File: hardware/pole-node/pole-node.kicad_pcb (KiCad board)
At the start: 2 copper layers, 50.5 x 33.5 mm, 31 parts, among them J1 Anderson, J2 RJ45, J3 Conn_01x02, J4 Conn_01x03, J5 Conn_01x03, J6 Conn_01x03, U1 AP3211, U2 MAX485E, U3 MAX485E

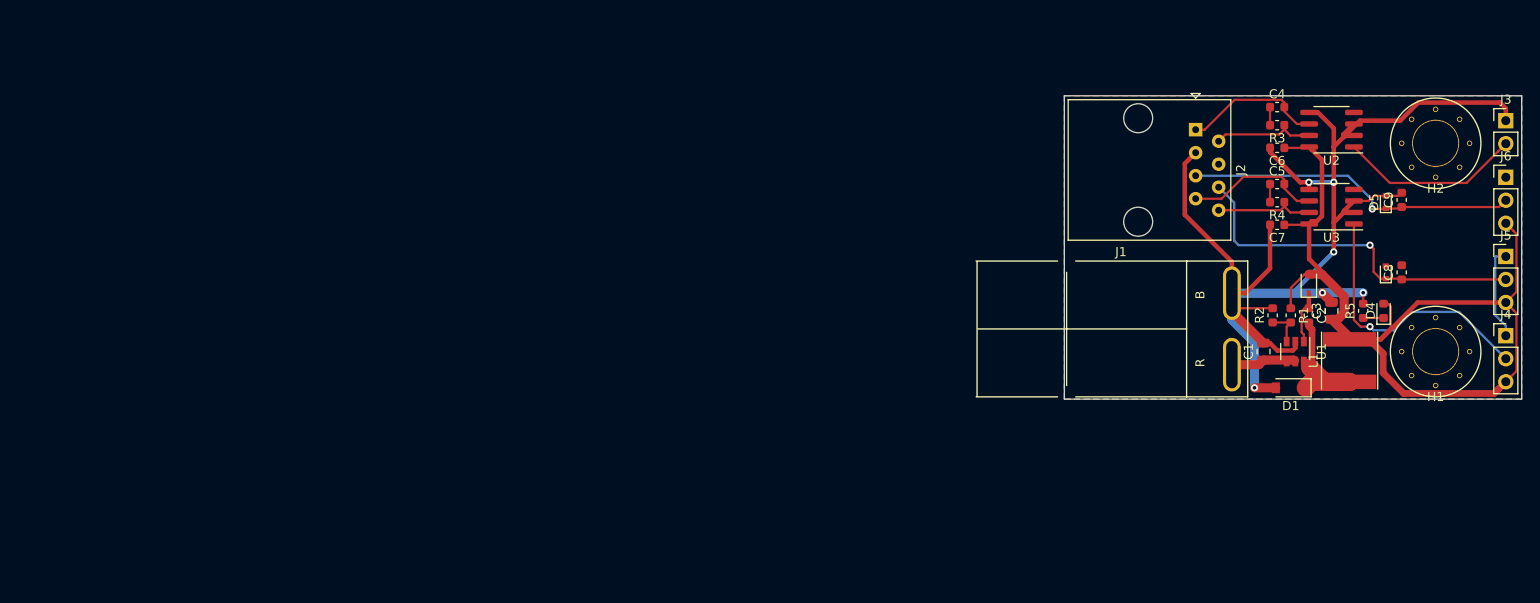
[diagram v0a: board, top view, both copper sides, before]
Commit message: Update pole node to v1.1
This adds lots of TVS diode, more decoupling, bulk caps on 5v and 12v
lines. Also adds pass-through Anderson connector.
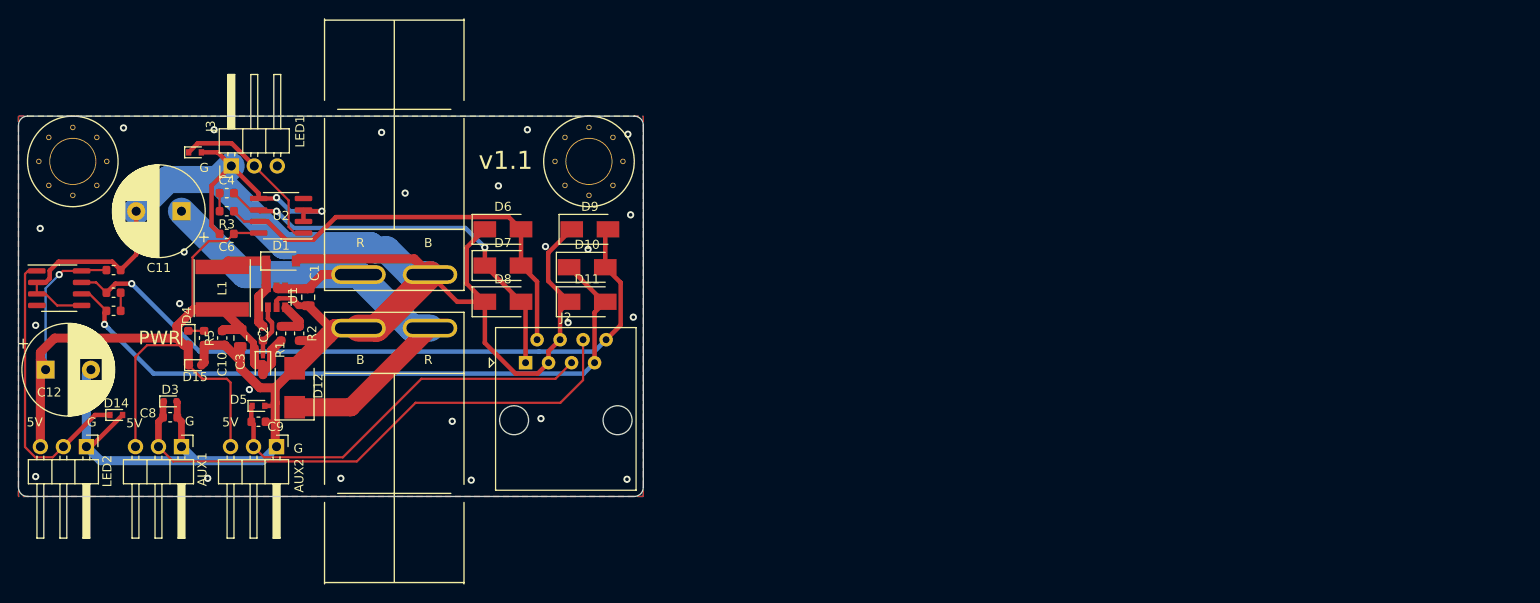
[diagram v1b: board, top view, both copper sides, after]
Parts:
- added C10: .1uF, Capacitor_SMD:C_0603_1608Metric, F.Cu at (60.0, 60.0)
- added C11: 470uF, Capacitor_THT:CP_Radial_D10.0mm_P5.00mm, F.Cu at (55.5, 46.0)
- added C12: 470uF, Capacitor_THT:CP_Radial_D10.0mm_P5.00mm, F.Cu at (40.5, 63.5)
- added D10: D_TVS_DATA, Diode_SMD:D_SMA, F.Cu at (100.3, 52.2)
- added D11: D_TVS_DATA, Diode_SMD:D_SMA, F.Cu at (100.3, 56.0)
- added D12: D_TVS_12V, Diode_SMD:D_SMB, F.Cu at (68.0, 65.5)
- added D13: D_TVS_5V, Diode_SMD:D_SOD-523, F.Cu at (57.0, 39.5)
- added D14: D_TVS_5V, Diode_SMD:D_SOD-523, F.Cu at (48.3, 68.5)
- added D15: D_TVS_5V, Diode_SMD:D_SOD-523, F.Cu at (57.0, 63.0)
- added D6: D_TVS_DATA, Diode_SMD:D_SMA, F.Cu at (91.0, 48.0)
- added D7: D_TVS_DATA, Diode_SMD:D_SMA, F.Cu at (91.0, 52.0)
- added D8: D_TVS_DATA, Diode_SMD:D_SMA, F.Cu at (91.0, 56.0)
- added D9: D_TVS_DATA, Diode_SMD:D_SMA, F.Cu at (100.6, 48.0)
- added J7: Anderson, homebrew:Anderson_1336G1_right_angle_bottom_two, F.Cu at (79.0, 53.0)
- D3, D5: value D_TVS -> D_TVS_5V
- J1: footprint homebrew:Anderson_1337G3_right_angle_bottom_two -> homebrew:Anderson_1336G1_right_angle_bottom_two
- J3: value Conn_01x02 -> Conn_01x03; footprint Connector_PinHeader_2.54mm:PinHeader_1x02_P2.54mm_Vertical -> Connector_PinHeader_2.54mm:PinHeader_1x03_P2.54mm_Horizontal
- J4, J5, J6: footprint Connector_PinHeader_2.54mm:PinHeader_1x03_P2.54mm_Vertical -> Connector_PinHeader_2.54mm:PinHeader_1x03_P2.54mm_Horizontal
- moved J4 157.2 mm to (45.0, 72.0), turned to 270 degrees
- moved H1 152.0 mm to (43.5, 40.5)
- moved J5 147.8 mm to (55.5, 72.0), turned to 270 degrees
- moved J3 140.8 mm to (61.0, 41.0), turned to 90 degrees
- moved U3 140.8 mm to (42.0, 54.5), turned to 0 degrees
- moved J6 139.0 mm to (66.0, 72.0), turned to 270 degrees
- moved C8 136.9 mm to (54.2, 68.8), turned to 0 degrees
- moved D3 135.0 mm to (54.2, 67.0), turned to 0 degrees
- moved D4 132.0 mm to (56.2, 60.0), turned to 270 degrees
- moved C5 129.3 mm to (48.0, 57.0), turned to 180 degrees
- moved R4 128.9 mm to (48.0, 55.0), turned to 0 degrees
- moved C9 128.6 mm to (64.0, 69.2), turned to 0 degrees
- moved C7 128.6 mm to (48.0, 52.5), turned to 0 degrees
- moved R5 128.0 mm to (58.0, 60.0), turned to 270 degrees
- moved D5 126.5 mm to (64.0, 67.5), turned to 0 degrees
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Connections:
- net Net-(C1-Pad1) renamed +12V
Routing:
- net GND: track 162.9 -> 261.1 mm, vias 6 -> 26
- net LED_2_B: track 10.9 -> 76.1 mm, vias 0 -> 1
- net LED_2_A: track 15.2 -> 74.8 mm, vias 0 -> 1
- net +12V: track 7.17 -> 61.0 mm
- net LED_1_B: track 11.3 -> 47.5 mm
- net LED_1_A: track 15.6 -> 44.8 mm, vias 0 -> 2
- net PIR1: track 39.9 -> 61.0 mm, vias 1 -> 0
- net +5V: track 106.2 -> 114.1 mm, vias 0 -> 1
- net PIR2: track 36.8 -> 44.6 mm, vias 1 -> 0
- net Net-(C2-Pad2): track 15.4 -> 12.5 mm
- net LED_1_OUT: track 20.7 -> 18.9 mm
- net LED_2_OUT: track 30.8 -> 32.3 mm, vias 1 -> 0
- net Net-(D4-Pad1): track 2.25 -> 1.75 mm
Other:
- board size 50.5 x 33.5 mm -> 69 x 42 mm
- rule pad_to_mask_clearance: 0.051 -> 0
- board text added: "1"
- board text added: "12v"
- board text added: "1A"
- board text added: "1B"
- board text added: "2"
- board text added: "2A"
- board text added: "2B"
- board text added: "AUX1"
- board text added: "AUX2"
- board text added: "PWR"
- board text added: "pole-node v1.1"
- board text added: "v1.1"
- board text removed: "PIR1"
- board text removed: "PIR2"
